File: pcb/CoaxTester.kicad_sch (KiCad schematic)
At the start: 51 parts

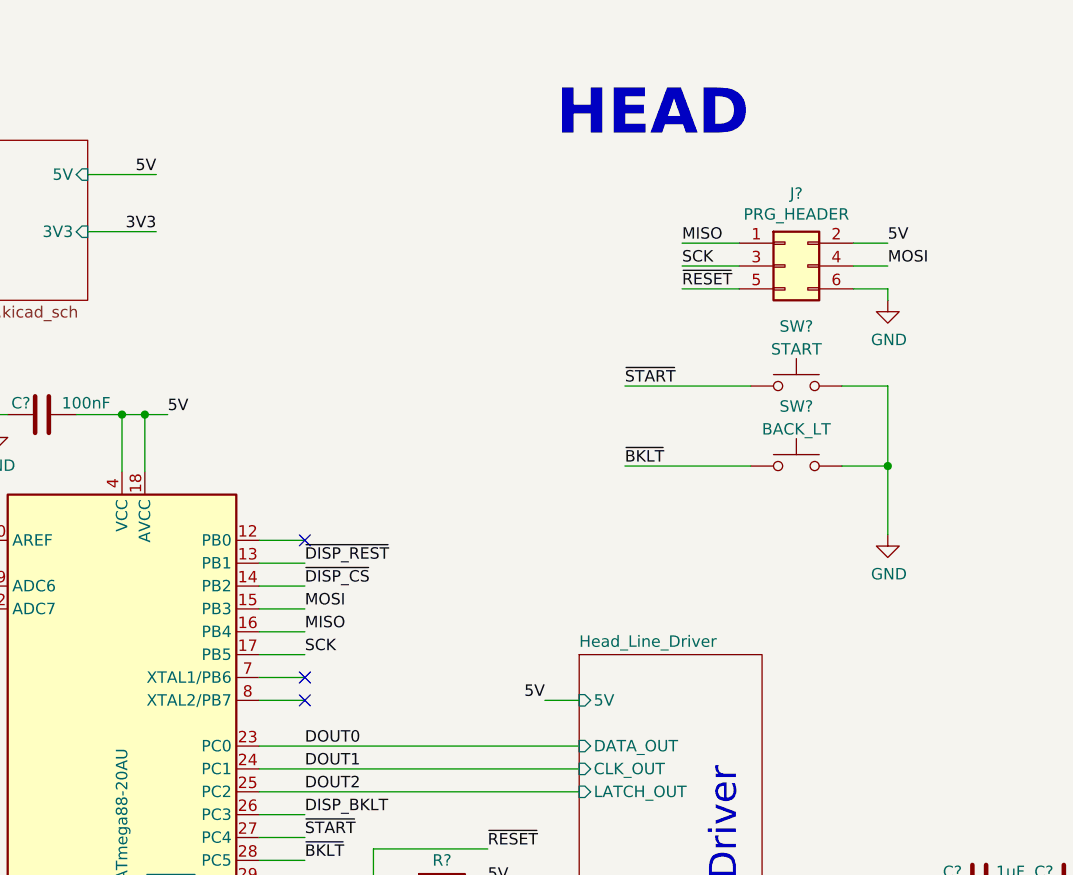
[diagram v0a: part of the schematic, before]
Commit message: Adds some controls and debounce.
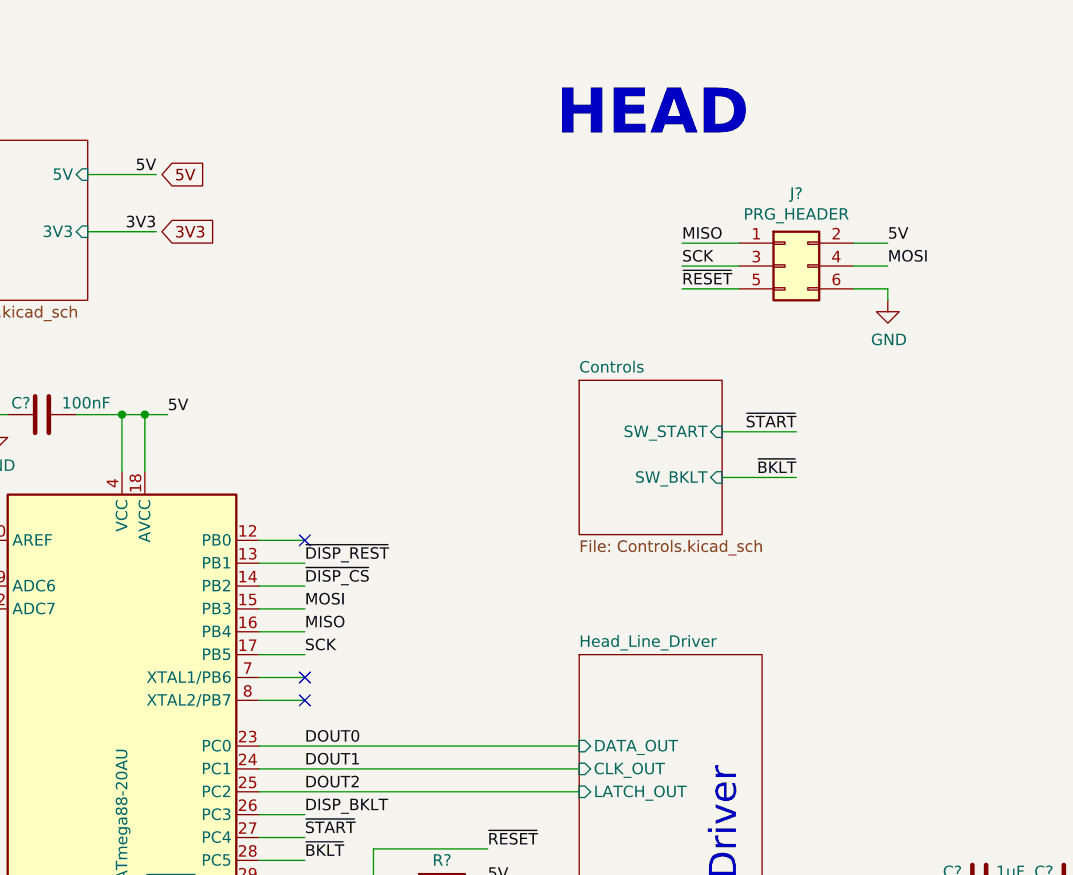
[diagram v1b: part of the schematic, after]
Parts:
- removed SW?: BACK_LT, Connector_PinHeader_2.54mm:PinHeader_1x02_P2.54mm_Vertical, symbol Switch:SW_Push
- removed SW?: START, Connector_PinHeader_2.54mm:PinHeader_1x02_P2.54mm_Vertical, symbol Switch:SW_Push
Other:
- added sheet Controls (Controls.kicad_sch)
- sheet Head_Line_Driver ports: added none; removed 5V

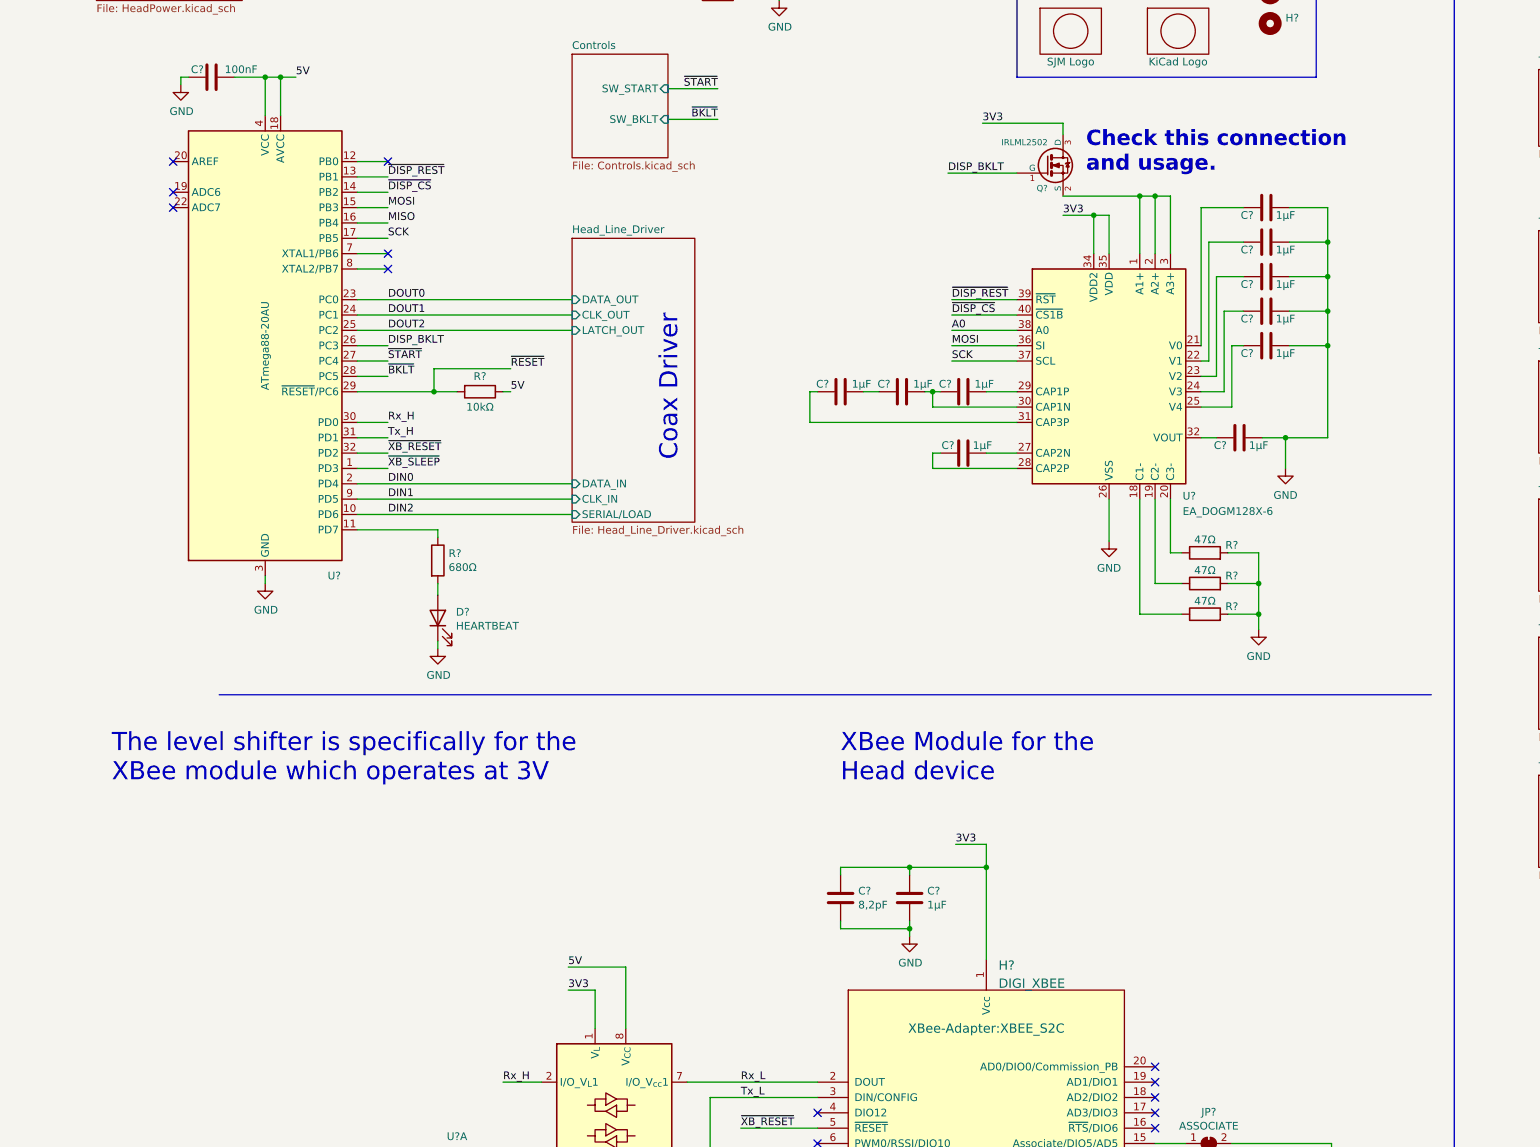
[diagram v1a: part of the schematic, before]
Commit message: Adds current control for the display adapter back light
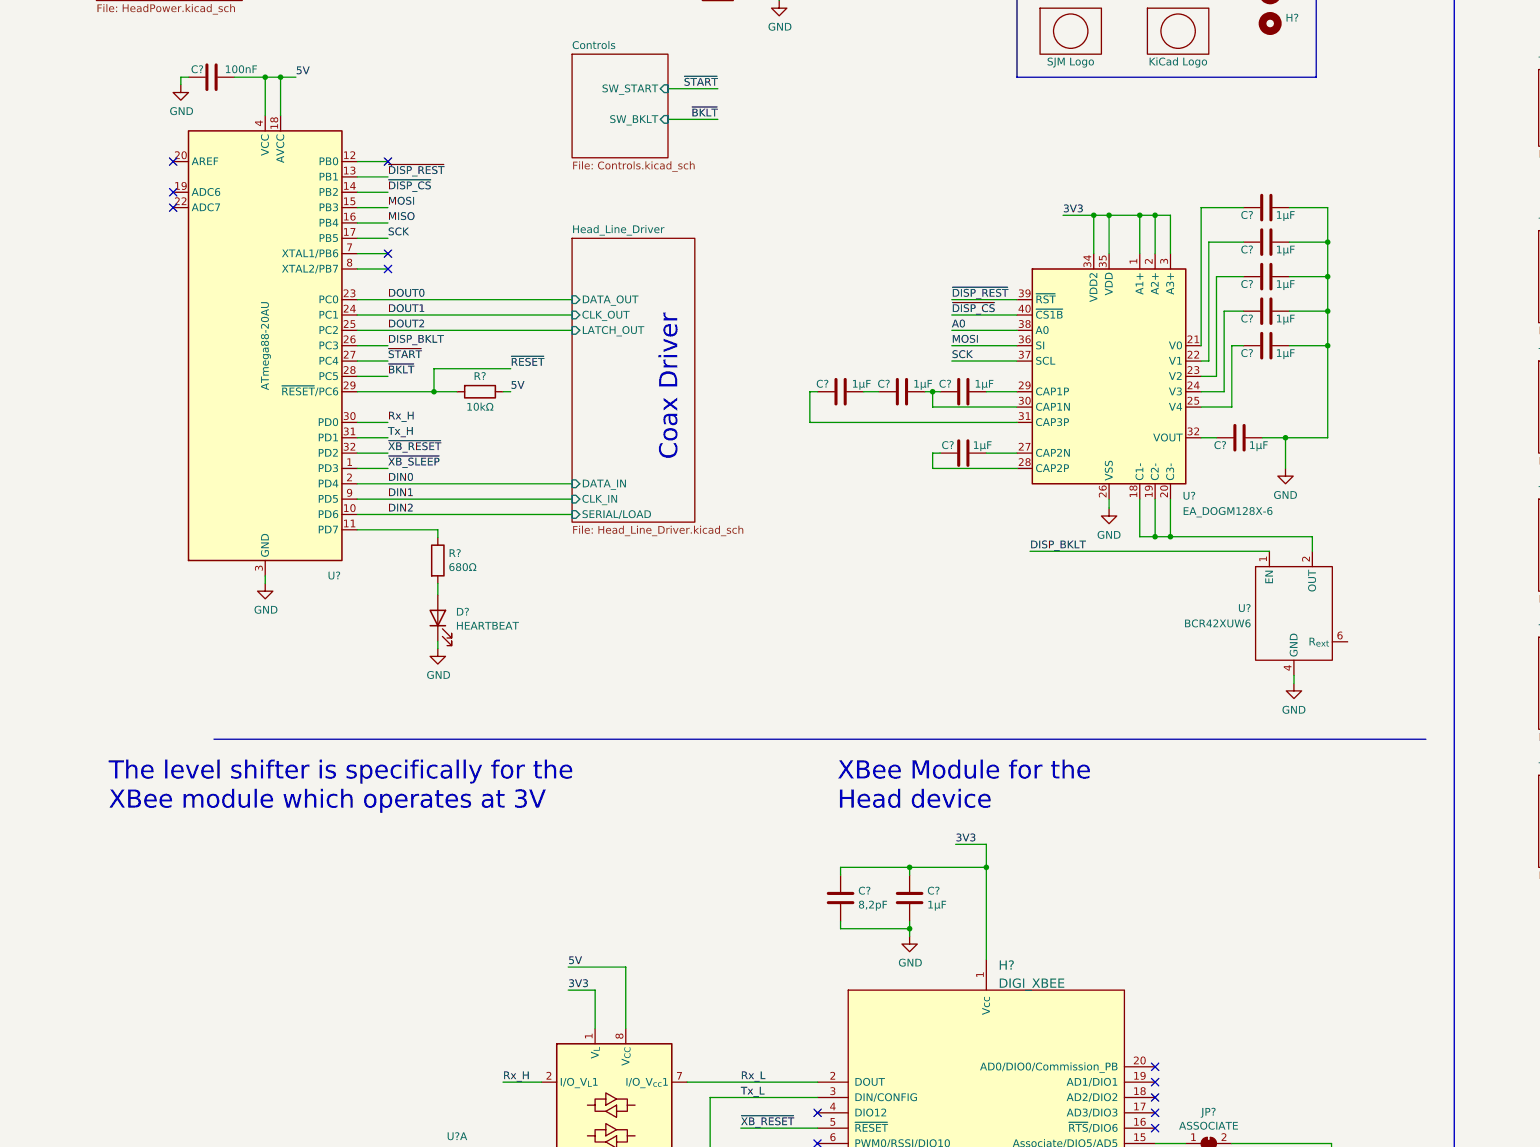
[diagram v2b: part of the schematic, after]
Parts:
- removed Q?: IRLML2502, tfac-footprints:Micro3, symbol Tfac-Symbols:IRLML2502
- removed R? (x3): 47Ω, Resistor_SMD:R_0805_2012Metric, symbol Device:R
- added U?: BCR42XUW6, Package_TO_SOT_SMD:SOT-23-6, symbol BCR42xUW6:BCR42XUW6
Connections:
- net 3V3: now also U?.1 (A1+), U?.2 (A2+), U?.3 (A3+)
- net DISP_BKLT: now also U?.1 (EN)
- net GND: now also U?.4 (GND)
- net at U?.20 (C3-): now also U?.18 (C1-), U?.19 (C2-), U?.2 (OUT), U?.3 (OUT), U?.5 (OUT)
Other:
- note removed: "Check this connection and usage."

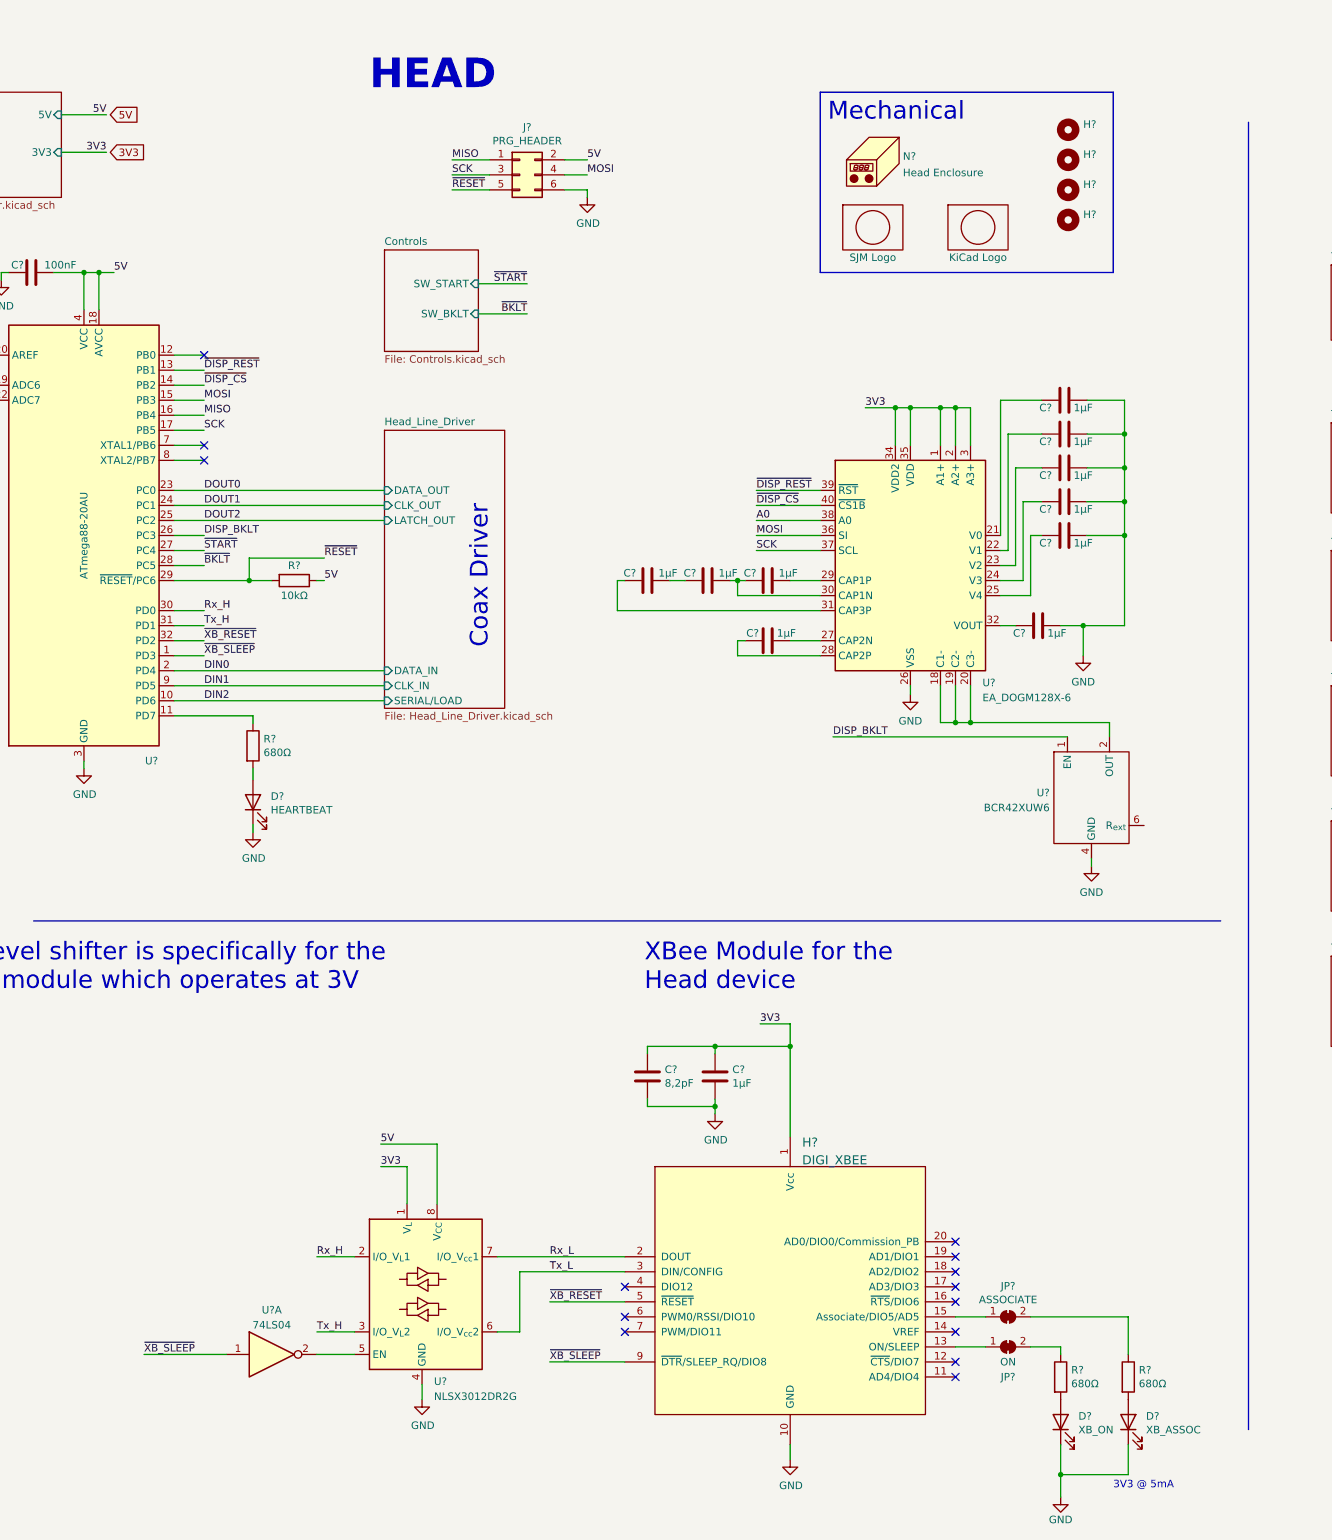
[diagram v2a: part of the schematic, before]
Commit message: Updates the schematic and fixes some symbols
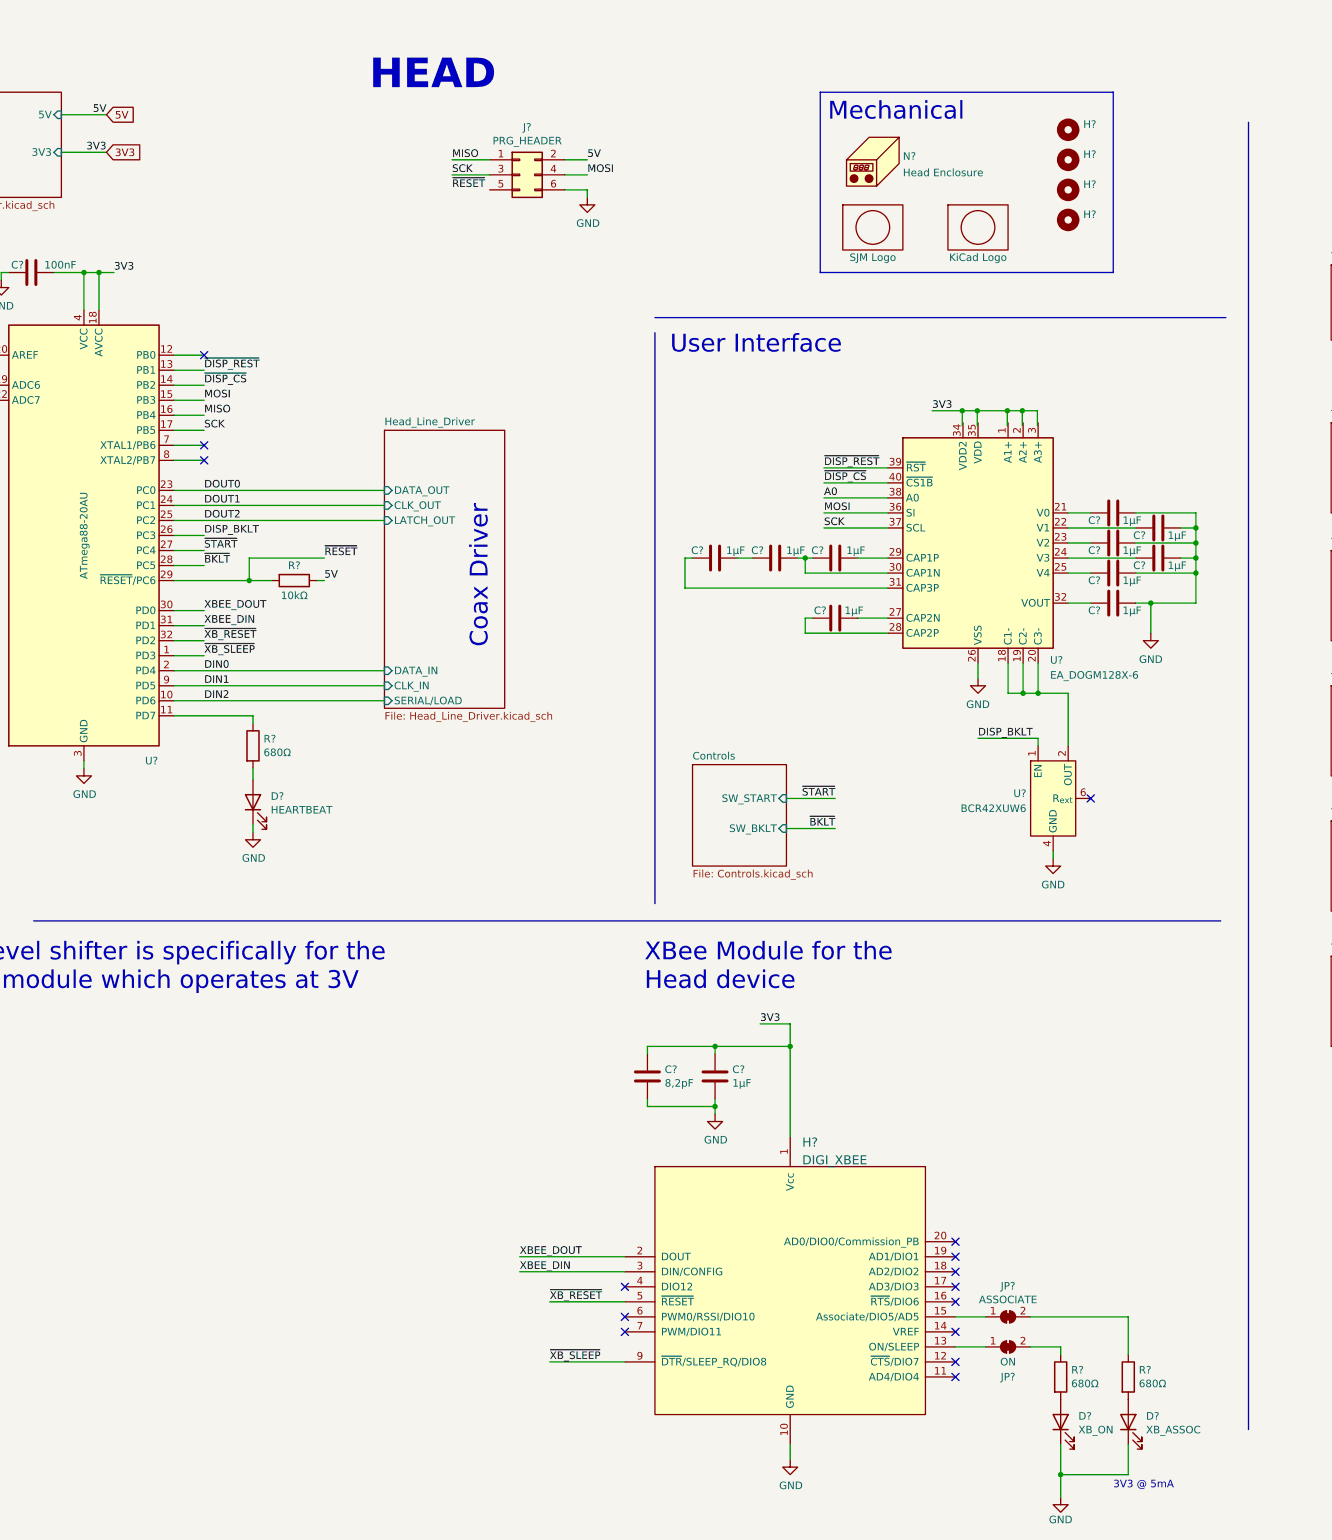
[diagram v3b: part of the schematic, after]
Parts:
- removed U?: NLSX3012DR2G, Package_SO:SOIC-8-N7_3.9x4.9mm_P1.27mm, symbol CoaxTester:NLSX3012DR2G
- removed U?: 74LS04, LED_Chain:SOIC-14, symbol 74xx:74LS04
- removed U?: BCR42XUW6, Package_TO_SOT_SMD:SOT-23-6, symbol BCR42xUW6:BCR42XUW6
- added U?: BCR42XUW6, Package_TO_SOT_SMD:SOT-23-6, symbol BCR42xUW6:BCR42XUW6
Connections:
- net Rx_L is gone; now on net XBEE_DOUT: H?.2 (DOUT)
- net Tx_L is gone; now on net XBEE_DIN: H?.3 (DIN/CONFIG)
- net 3V3: now also C?.2, U?.18 (AVCC), U?.4 (VCC), U?.6 (VCC); no longer U?.1 (A1+), U?.2 (A2+), U?.3 (A3+), U?.34 (VDD2), U?.35 (VDD)
- net 5V: no longer C?.2, U?.18 (AVCC), U?.4 (VCC), U?.6 (VCC)
- net DISP_BKLT: now also U?.1 (EN)
- net GND: now also U?.4 (GND)
- net ~{RESET}: no longer J?.5 (Pin_5)
- net at U?.18 (C1-), U?.19 (C2-), U?.20 (C3-): now also U?.2 (OUT), U?.3 (OUT), U?.5 (OUT)
- net Rx_H renamed XBEE_DOUT
- net Tx_H renamed XBEE_DIN
- no-connect marks 27 -> 28
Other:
- note added: "User Interface"
- moved on the sheet: C?, U?
